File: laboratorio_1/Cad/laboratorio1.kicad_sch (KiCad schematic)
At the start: 16 parts, among them J1 Conn_Coaxial, J2 Conn_Coaxial, J3 +12V, J4 GND, J5 -12 V, U1 LM741, U2 LM741, U3 LM741

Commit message: Actualizacion laboratorio 1
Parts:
- removed J1, J2: Conn_Coaxial, symbol Connector:Conn_Coaxial
- removed J3: +12V, symbol Connector:Conn_01x01_Pin
- removed J4: GND, symbol Connector:Conn_01x01_Pin
- removed J5: -12 V, symbol Connector:Conn_01x01_Pin
- removed U1, U2, U3: LM741, symbol Amplifier_Operational:LM741
- added U1: TL084, symbol Amplifier_Operational:TL084
- added j1: Vdd, symbol Connector:Screw_Terminal_01x01
- added j2: Vss, symbol Connector:Screw_Terminal_01x01
- added j3: GND, symbol Connector:Screw_Terminal_01x01
- added j4: Input, symbol Connector:Conn_Coaxial
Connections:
- net GND: now also U1.10 (+), U1.12 (+), U1.3 (+), U1.5 (+), j3.1 (Pin_1), j4.2 (Ext)
- net at R3.2: now also C2.1, U1.9 (-); no longer R5.1
- net at R4.2, R5.2: now also U1.8
- net at R4.1: now also C1.1, R1.2, R2.1, U1.2 (-); no longer C2.2
- net at C1.2, R2.2: now also R3.1, U1.1; no longer R6.1
- net at R6.2: now also R5.1, U1.6 (-); no longer C2.1
- net at R1.1: now also j4.1 (In)
- new net: U1.11 (V-), j2.1 (Pin_1)
- new net: U1.4 (V+), j1.1 (Pin_1)
- new net: U1.13 (-), U1.14
- new net: C2.2, R6.1, U1.7
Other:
- note added: "El operacional no se utiliza, y para no dejarlo flotando, lo coloco como un seguidor de 0 V"

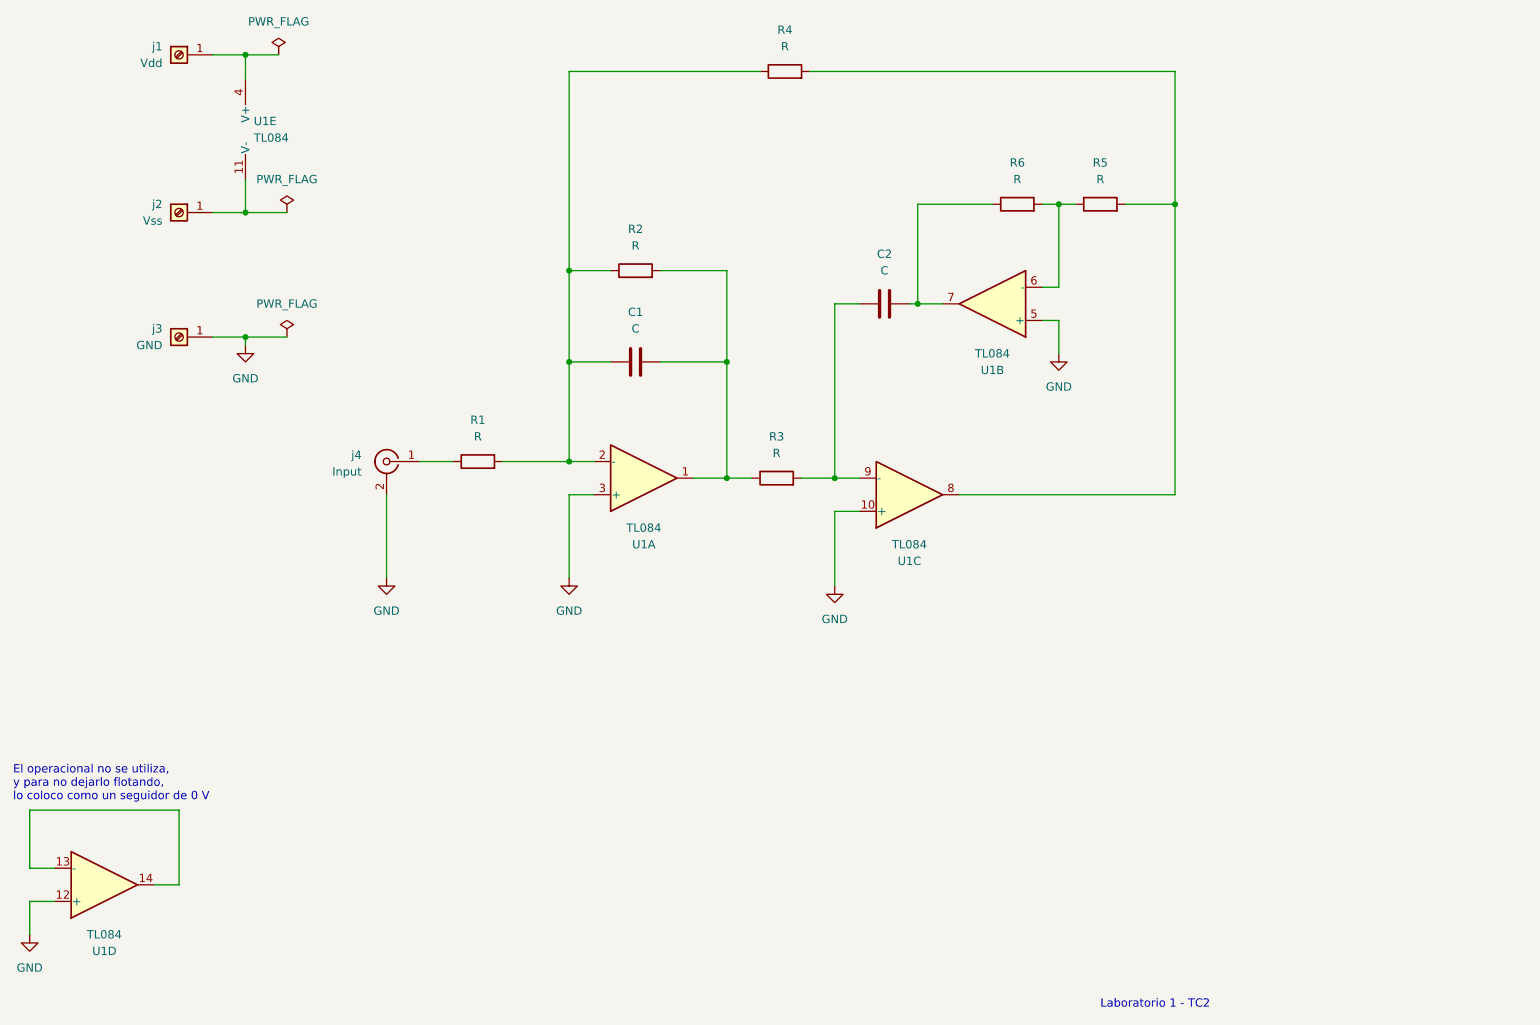
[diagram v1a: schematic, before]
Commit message: actualizo LTSpice, y Kicad
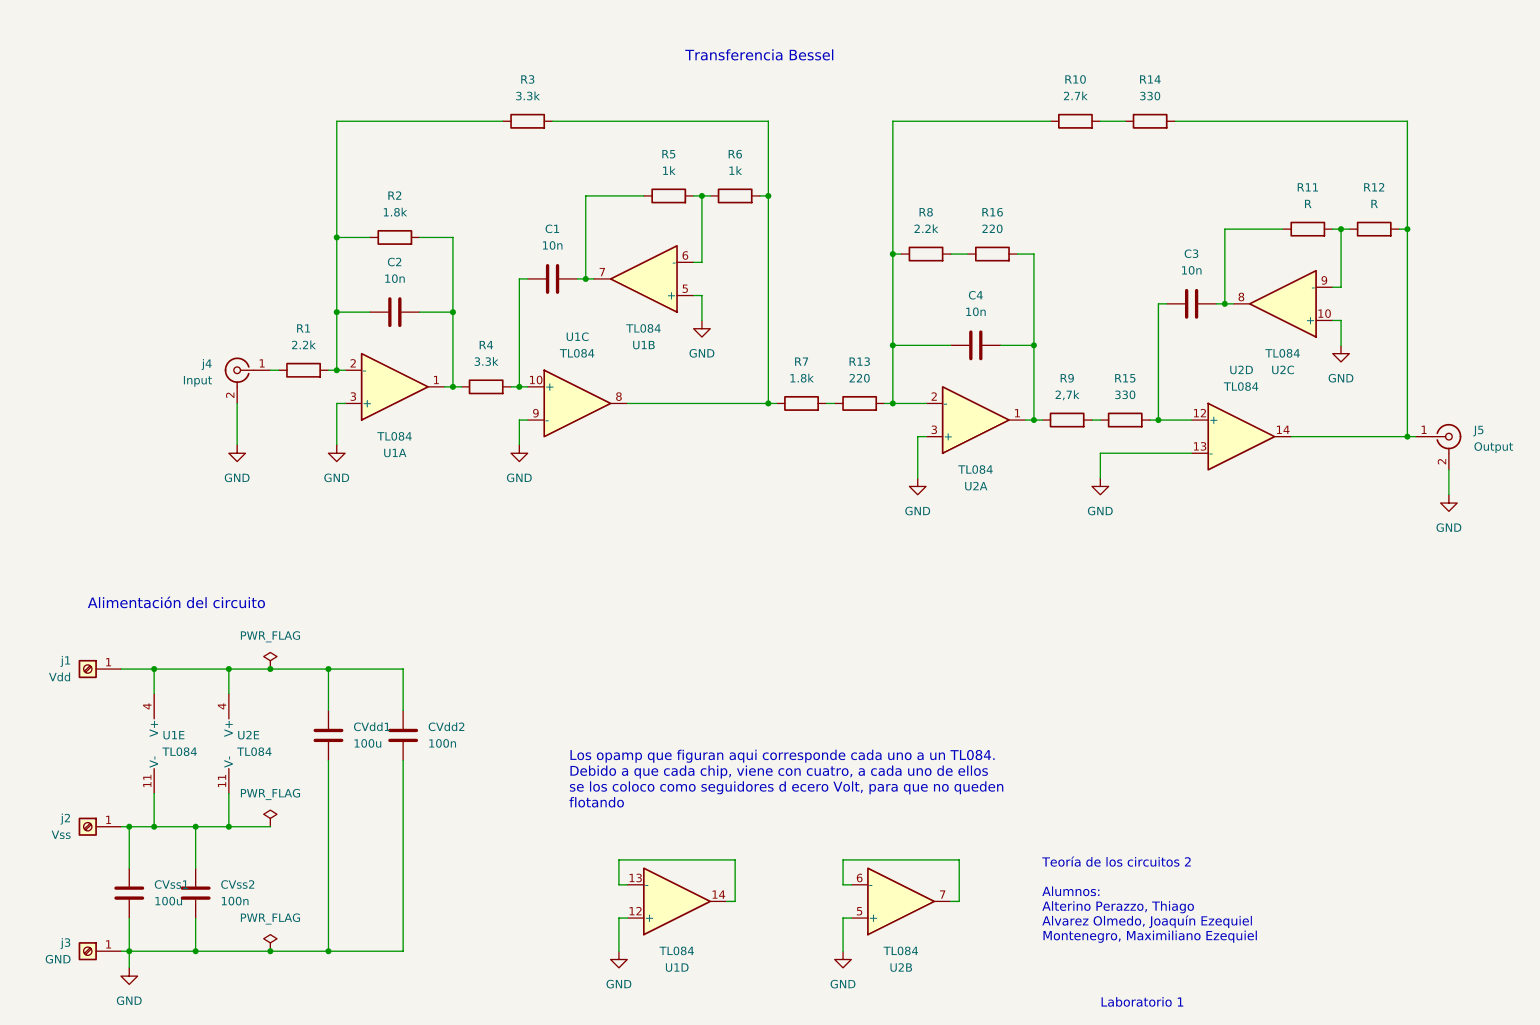
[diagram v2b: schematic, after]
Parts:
- added C3, C4: 10n, Capacitor_THT:C_Rect_L7.2mm_W2.5mm_P5.00mm_FKS2_FKP2_MKS2_MKP2, symbol Device:C
- added CVdd1, CVss1: 100u, Capacitor_THT:C_Radial_D8.0mm_H11.5mm_P3.50mm, symbol Device:C
- added CVdd2, CVss2: 100n, Capacitor_THT:C_Disc_D5.0mm_W2.5mm_P5.00mm, symbol Device:C
- added J5: Output, Connector_Coaxial:BNC_TEConnectivity_1478035_Horizontal, symbol Connector:Conn_Coaxial
- added R10: 2.7k, Resistor_THT:R_Axial_DIN0207_L6.3mm_D2.5mm_P10.16mm_Horizontal, symbol Device:R
- added R11, R12: R, Resistor_THT:R_Axial_DIN0207_L6.3mm_D2.5mm_P10.16mm_Horizontal, symbol Device:R
- added R13, R16: 220, Resistor_THT:R_Axial_DIN0207_L6.3mm_D2.5mm_P10.16mm_Horizontal, symbol Device:R
- added R14, R15: 330, Resistor_THT:R_Axial_DIN0207_L6.3mm_D2.5mm_P10.16mm_Horizontal, symbol Device:R
- added R7: 1.8k, Resistor_THT:R_Axial_DIN0207_L6.3mm_D2.5mm_P10.16mm_Horizontal, symbol Device:R
- added R8: 2.2k, Resistor_THT:R_Axial_DIN0207_L6.3mm_D2.5mm_P10.16mm_Horizontal, symbol Device:R
- added R9: 2,7k, Resistor_THT:R_Axial_DIN0207_L6.3mm_D2.5mm_P10.16mm_Horizontal, symbol Device:R
- added U2: TL084, Package_DIP:CERDIP-14_W7.62mm_SideBrazed_LongPads_Socket, symbol Amplifier_Operational:TL084
- C1, C2: value C -> 10n; footprint (none) -> Capacitor_THT:C_Rect_L7.2mm_W2.5mm_P5.00mm_FKS2_FKP2_MKS2_MKP2
- R1: value R -> 2.2k; footprint (none) -> Resistor_THT:R_Axial_DIN0207_L6.3mm_D2.5mm_P10.16mm_Horizontal
- R2: value R -> 1.8k; footprint (none) -> Resistor_THT:R_Axial_DIN0207_L6.3mm_D2.5mm_P10.16mm_Horizontal
- R3, R4: value R -> 3.3k; footprint (none) -> Resistor_THT:R_Axial_DIN0207_L6.3mm_D2.5mm_P10.16mm_Horizontal
- R5, R6: value R -> 1k; footprint (none) -> Resistor_THT:R_Axial_DIN0207_L6.3mm_D2.5mm_P10.16mm_Horizontal
- U1: footprint (none) -> Package_DIP:CERDIP-14_W7.62mm_SideBrazed_LongPads_Socket
- j1: footprint (none) -> Connector:Banana_Cliff_FCR7350R_S16N-PC_Horizontal
- j2: footprint (none) -> Connector:Banana_Cliff_FCR7350L_S16N-PC_Horizontal
- j3: footprint (none) -> Connector:Banana_Cliff_FCR7350G_S16N-PC_Horizontal
- j4: footprint (none) -> Connector_Coaxial:BNC_TEConnectivity_1478035_Horizontal
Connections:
- net GND: now also U1.9 (-), CVdd1.2, CVdd2.2, CVss1.2, CVss2.2, J5.2 (Ext), U2.10 (+), U2.13 (-), U2.3 (+), U2.5 (+); no longer U1.10 (+)
- net at R1.2, R2.1, U1.2 (-): now also C2.1, R3.1; no longer C1.1, R4.1
- net at R2.2, U1.1: now also C2.2, R4.1; no longer C1.2, R3.1
- net at U1.11 (V-), j2.1 (Pin_1): now also CVss1.1, CVss2.1, U2.11 (V-)
- net at U1.4 (V+), j1.1 (Pin_1): now also CVdd1.1, CVdd2.1, U2.4 (V+)
- new net: R16.1, R8.2
- new net: C4.2, R16.2, R9.1, U2.1
- new net: J5.1 (In), R12.2, R14.2, U2.14
- new net: C1.1, R4.2, U1.10 (+)
- new net: R3.2, R6.2, R7.1, U1.8
- new net: C4.1, R10.1, R13.2, R8.1, U2.2 (-)
- new net: C3.1, R15.2, U2.12 (+)
- new net: C3.2, R11.1, U2.8
- new net: C1.2, R5.1, U1.7
- new net: R5.2, R6.1, U1.6 (-)
- new net: U2.6 (-), U2.7
- new net: R11.2, R12.1, U2.9 (-)
- new net: R10.2, R14.1
- new net: R15.1, R9.2
- new net: R13.1, R7.2
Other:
- note added: "Alimentación del circuito"
- note added: "Laboratorio 1"
- note added: "Los opamp que figuran aqui corresponde cada uno a un TL084. Debido a que cada chip, viene con cuatro, a cada uno de ellos se los coloco como seguidores d ecero Volt, para que no queden flotando"
- note added: "Teoría de los circuitos 2 Alumnos: Alterino Perazzo, Thiago Alvarez Olmedo, Joaquín Ezequiel Montenegro, Maximiliano Ezequiel"
- note added: "Transferencia Bessel"
- note removed: "El operacional no se utiliza, y para no dejarlo flotando, lo coloco como un seguidor de 0 V"
- note removed: "Laboratorio 1 - TC2"
- moved on the sheet: j1, j2, j3, j4

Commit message: ahora si actualizo con windows el kicad
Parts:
- R11, R12: value R -> 1k

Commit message: ggregue Jumper al Cad
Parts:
- added J6: VA1, Connector_PinHeader_1.00mm:PinHeader_1x01_P1.00mm_Vertical, symbol Connector:Screw_Terminal_01x01
- added J7: Vin, Connector_PinHeader_1.00mm:PinHeader_1x01_P1.00mm_Vertical, symbol Connector:Screw_Terminal_01x01
- added J8: Vout, Connector_PinHeader_1.00mm:PinHeader_1x01_P1.00mm_Vertical, symbol Connector:Screw_Terminal_01x01
- added J9: Masa, Connector_PinHeader_1.00mm:PinHeader_1x03_P1.00mm_Vertical, symbol Connector:Screw_Terminal_01x03
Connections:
- net GND: now also J9.1 (Pin_1), J9.2 (Pin_2), J9.3 (Pin_3)
- net at R1.1, j4.1 (In): now also J7.1 (Pin_1)
- net at J5.1 (In), R12.2, R14.2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: now also J8.1 (Pin_1)
- net at R3.2, R6.2, R7.1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: now also J6.1 (Pin_1)
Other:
- moved on the sheet: j4

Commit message: actualizo desde linux
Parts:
- C1, C2, C3, C4: footprint Capacitor_THT:C_Rect_L7.2mm_W2.5mm_P5.00mm_FKS2_FKP2_MKS2_MKP2 -> Capacitor_THT:C_Rect_L11.0mm_W3.4mm_P10.00mm_MKT
- CVdd2, CVss2: footprint Capacitor_THT:C_Disc_D5.0mm_W2.5mm_P5.00mm -> Capacitor_THT:C_Disc_D5.0mm_W2.5mm_P2.50mm
- j1: footprint Connector:Banana_Cliff_FCR7350R_S16N-PC_Horizontal -> Connector:Banana_Jack_1Pin
- j2: footprint Connector:Banana_Cliff_FCR7350L_S16N-PC_Horizontal -> Connector:Banana_Jack_1Pin
- j3: footprint Connector:Banana_Cliff_FCR7350G_S16N-PC_Horizontal -> Connector:Banana_Jack_1Pin
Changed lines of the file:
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@@
 			)
 		)
-		(property "Footprint" "Capacitor_THT:C_Disc_D5.0mm_W2.5mm_P5.00mm"
+		(property "Footprint" "Capacitor_THT:C_Disc_D5.0mm_W2.5mm_P2.50mm"
 			(at 50.4952 176.53 0)
 			(effects
@@
 			)
 		)
-		(property "Footprint" "Capacitor_THT:C_Disc_D5.0mm_W2.5mm_P5.00mm"
+		(property "Footprint" "Capacitor_THT:C_Disc_D5.0mm_W2.5mm_P2.50mm"
 			(at 82.2452 152.4 0)
 			(effects
@@
 			)
 		)
-		(property "Footprint" "Capacitor_THT:C_Rect_L7.2mm_W2.5mm_P5.00mm_FKS2_FKP2_MKS2_MKP2"
+		(property "Footprint" "Capacitor_THT:C_Rect_L11.0mm_W3.4mm_P10.00mm_MKT"
 			(at 205.74 81.5848 0)
 			(effects
@@
 			)
 		)
-		(property "Footprint" "Connector:Banana_Cliff_FCR7350G_S16N-PC_Horizontal"
+		(property "Footprint" "Connector:Banana_Jack_1Pin"
 			(at 33.02 181.61 0)
 			(effects
@@
 			)
 		)
-		(property "Footprint" "Capacitor_THT:C_Rect_L7.2mm_W2.5mm_P5.00mm_FKS2_FKP2_MKS2_MKP2"
+		(property "Footprint" "Capacitor_THT:C_Rect_L11.0mm_W3.4mm_P10.00mm_MKT"
 			(at 83.82 82.8548 0)
 			(effects
@@
 			)
 		)
-		(property "Footprint" "Capacitor_THT:C_Rect_L7.2mm_W2.5mm_P5.00mm_FKS2_FKP2_MKS2_MKP2"
+		(property "Footprint" "Capacitor_THT:C_Rect_L11.0mm_W3.4mm_P10.00mm_MKT"
 			(at 107.95 77.7748 0)
 			(effects
@@
 			)
 		)
-		(property "Footprint" "Connector:Banana_Cliff_FCR7350L_S16N-PC_Horizontal"
+		(property "Footprint" "Connector:Banana_Jack_1Pin"
 			(at 33.02 162.56 0)
 			(effects
@@
 			)
 		)
-		(property "Footprint" "Capacitor_THT:C_Rect_L7.2mm_W2.5mm_P5.00mm_FKS2_FKP2_MKS2_MKP2"
+		(property "Footprint" "Capacitor_THT:C_Rect_L11.0mm_W3.4mm_P10.00mm_MKT"
 			(at 172.72 87.9348 0)
 			(effects
@@
 			)
 		)
-		(property "Footprint" "Connector:Banana_Cliff_FCR7350R_S16N-PC_Horizontal"
+		(property "Footprint" "Connector:Banana_Jack_1Pin"
 			(at 33.02 138.43 0)
 			(effects

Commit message: última actualización del get, modifcación completa del pcb
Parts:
- removed J6: VA1, Connector_PinHeader_1.00mm:PinHeader_1x01_P1.00mm_Vertical, symbol Connector:Screw_Terminal_01x01
- removed J7: Vin, Connector_PinHeader_1.00mm:PinHeader_1x01_P1.00mm_Vertical, symbol Connector:Screw_Terminal_01x01
- removed J8: Vout, Connector_PinHeader_1.00mm:PinHeader_1x01_P1.00mm_Vertical, symbol Connector:Screw_Terminal_01x01
- J5, j4: footprint Connector_Coaxial:BNC_TEConnectivity_1478035_Horizontal -> Connector_Coaxial:BNC_Amphenol_B6252HB-NPP3G-50_Horizontal
